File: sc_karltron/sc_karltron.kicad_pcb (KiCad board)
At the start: 2 copper layers, 88.6 x 50.6 mm, 6 parts, among them J1 Conn_01x02, J2 Conn_01x02

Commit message: basic components
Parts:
- added C1: C, Capacitor_THT:C_Disc_D5.0mm_W2.5mm_P5.00mm, F.Cu at (171.6, 25.9)
- added C2: C, Capacitor_THT:C_Disc_D5.0mm_W2.5mm_P5.00mm, F.Cu at (178.0, 10.4)
- added C3: C, Capacitor_THT:C_Disc_D5.0mm_W2.5mm_P5.00mm, F.Cu at (176.8, 18.6)
- added C4: C, Capacitor_THT:C_Disc_D5.0mm_W2.5mm_P5.00mm, F.Cu at (162.8, 29.9)
- added C5: C, Capacitor_THT:C_Disc_D5.0mm_W2.5mm_P5.00mm, F.Cu at (163.4, 25.9)
- added C6: C_Polarized, Capacitor_THT:CP_Radial_D5.0mm_P2.50mm, F.Cu at (152.5, 39.3)
- added R1: 100K, Resistor_THT:R_Axial_DIN0207_L6.3mm_D2.5mm_P10.16mm_Horizontal, F.Cu at (138.7, 49.5)
- added R10: 100K, Resistor_THT:R_Axial_DIN0207_L6.3mm_D2.5mm_P10.16mm_Horizontal, F.Cu at (164.7, 14.5)
- added R11: LDR, Resistor_THT:R_Axial_DIN0207_L6.3mm_D2.5mm_P10.16mm_Horizontal, F.Cu at (122.9, 33.2)
- added R12: 10K, Resistor_THT:R_Axial_DIN0207_L6.3mm_D2.5mm_P10.16mm_Horizontal, F.Cu at (136.8, 21.9)
- added R13: 100K, Resistor_THT:R_Axial_DIN0207_L6.3mm_D2.5mm_P10.16mm_Horizontal, F.Cu at (150.1, 21.9)
- added R14: 10K, Resistor_THT:R_Axial_DIN0207_L6.3mm_D2.5mm_P10.16mm_Horizontal, F.Cu at (125.3, 45.4)
- added R15: 100K, Resistor_THT:R_Axial_DIN0207_L6.3mm_D2.5mm_P10.16mm_Horizontal, F.Cu at (136.2, 37.3)
- added R16: 1M, Resistor_THT:R_Axial_DIN0207_L6.3mm_D2.5mm_P10.16mm_Horizontal, F.Cu at (149.5, 29.9)
- added R17: 100K, Resistor_THT:R_Axial_DIN0207_L6.3mm_D2.5mm_P10.16mm_Horizontal, F.Cu at (122.9, 41.4)
- added R18: 1M, Resistor_THT:R_Axial_DIN0207_L6.3mm_D2.5mm_P10.16mm_Horizontal, F.Cu at (112.0, 49.2)
- added R19: 100K, Resistor_THT:R_Axial_DIN0207_L6.3mm_D2.5mm_P10.16mm_Horizontal, F.Cu at (150.1, 25.9)
- added R2: 100K, Resistor_THT:R_Axial_DIN0207_L6.3mm_D2.5mm_P10.16mm_Horizontal, F.Cu at (138.7, 41.4)
- added R20: 1M, Resistor_THT:R_Axial_DIN0207_L6.3mm_D2.5mm_P10.16mm_Horizontal, F.Cu at (125.3, 49.5)
- added R3: 100K, Resistor_THT:R_Axial_DIN0207_L6.3mm_D2.5mm_P10.16mm_Horizontal, F.Cu at (122.9, 37.3)
- added R4: LDR, Resistor_THT:R_Axial_DIN0207_L6.3mm_D2.5mm_P10.16mm_Horizontal, F.Cu at (163.4, 21.9)
- added R5: 10K, Resistor_THT:R_Axial_DIN0207_L6.3mm_D2.5mm_P10.16mm_Horizontal, F.Cu at (136.2, 33.2)
- added R6: 100K, Resistor_THT:R_Axial_DIN0207_L6.3mm_D2.5mm_P10.16mm_Horizontal, F.Cu at (138.7, 45.4)
- added R7: 10K, Resistor_THT:R_Axial_DIN0207_L6.3mm_D2.5mm_P10.16mm_Horizontal, F.Cu at (136.8, 25.9)
- added R8: LDR, Resistor_THT:R_Axial_DIN0207_L6.3mm_D2.5mm_P10.16mm_Horizontal, F.Cu at (164.7, 10.4)
- added R9: 10K, Resistor_THT:R_Axial_DIN0207_L6.3mm_D2.5mm_P10.16mm_Horizontal, F.Cu at (149.5, 34.0)
- added RV1: B100K, Potentiometer_THT:Potentiometer_ACP_CA9-V10_Vertical, F.Cu at (151.2, 16.6)
- added RV2: B100K, Potentiometer_THT:Potentiometer_ACP_CA9-V10_Vertical, F.Cu at (123.3, 16.6)
- added RV3: B100K, Potentiometer_THT:Potentiometer_ACP_CA9-V10_Vertical, F.Cu at (137.2, 16.6)
- added RV4: B100K, Potentiometer_THT:Potentiometer_ACP_CA9-V10_Vertical, F.Cu at (123.3, 28.0)
- added U1: TL074, Package_DIP:DIP-14_W7.62mm, F.Cu at (112.1, 29.9)
- added U2: TL074, Package_DIP:DIP-14_W7.62mm, F.Cu at (112.1, 10.5)

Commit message: working too
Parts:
- added D1: LED, LED_THT:LED_D5.0mm_Horizontal_O3.81mm_Z3.0mm, F.Cu at (107.6, 73.2)
- added D2: LED, LED_THT:LED_D5.0mm_Horizontal_O3.81mm_Z3.0mm, F.Cu at (116.0, 73.2)
- added D3: LED, LED_THT:LED_D5.0mm_Horizontal_O3.81mm_Z3.0mm, F.Cu at (126.5, 73.7)
- added J3: In1, Connector_PinHeader_2.54mm:PinHeader_1x02_P2.54mm_Vertical, F.Cu at (216.6, 16.5)
- added J4: Out1, Connector_PinHeader_2.54mm:PinHeader_1x02_P2.54mm_Vertical, F.Cu at (227.7, 16.5)
- added J5: Out2, Connector_PinHeader_2.54mm:PinHeader_1x02_P2.54mm_Vertical, F.Cu at (190.3, 48.1)
- added J6: In2, Connector_PinHeader_2.54mm:PinHeader_1x02_P2.54mm_Vertical, F.Cu at (205.4, 16.5)
- added J7: Out3, Connector_PinHeader_2.54mm:PinHeader_1x02_P2.54mm_Vertical, F.Cu at (227.7, 31.7)
- added J8: Out4, Connector_PinHeader_2.54mm:PinHeader_1x02_P2.54mm_Vertical, F.Cu at (238.8, 16.5)
- added J9: In3, Connector_PinHeader_2.54mm:PinHeader_1x02_P2.54mm_Vertical, F.Cu at (181.5, 45.4)
- added R21: RLED, Resistor_THT:R_Axial_DIN0207_L6.3mm_D2.5mm_P10.16mm_Horizontal, F.Cu at (104.2, 84.4)
- added R22: RLED, Resistor_THT:R_Axial_DIN0207_L6.3mm_D2.5mm_P10.16mm_Horizontal, F.Cu at (113.0, 84.1)
- added R23: RLED, Resistor_THT:R_Axial_DIN0207_L6.3mm_D2.5mm_P10.16mm_Horizontal, F.Cu at (123.2, 84.2)
- added RV5: B100K, Potentiometer_THT:Potentiometer_Alpha_RD901F-40-00D_Single_Vertical, F.Cu at (147.4, 70.0)
- added RV6: B100K, Potentiometer_THT:Potentiometer_Alpha_RD901F-40-00D_Single_Vertical, F.Cu at (177.9, 98.2)
- added RV7: B100K, Potentiometer_THT:Potentiometer_Alpha_RD901F-40-00D_Single_Vertical, F.Cu at (163.5, 70.4)
- added RV8: B100K, Potentiometer_THT:Potentiometer_Alpha_RD901F-40-00D_Single_Vertical, F.Cu at (178.6, 70.7)
- C4, C5: value C -> 100nF
- C6: value C_Polarized -> 10uF
- J1, J2: footprint Connector_PinHeader_2.54mm:PinHeader_1x02_P2.54mm_Vertical -> Connector_PinHeader_2.54mm:PinHeader_1x02_P2.54mm_Horizontal
- R11, R4, R8: footprint Resistor_THT:R_Axial_DIN0207_L6.3mm_D2.5mm_P10.16mm_Horizontal -> Resistor_THT:R_Axial_DIN0204_L3.6mm_D1.6mm_P5.08mm_Horizontal
- RV1, RV2, RV3, RV4: footprint Potentiometer_THT:Potentiometer_ACP_CA9-V10_Vertical -> Potentiometer_THT:Potentiometer_ACP_CA9-H5_Horizontal
- moved R8 88.7 mm to (125.4, 90.0)
- moved U2 85.5 mm to (120.7, 95.6)
- moved R4 82.9 mm to (115.8, 89.8)
- moved U1 79.5 mm to (158.1, 94.8)
- moved C6 75.3 mm to (144.4, 114.2), turned to 90 degrees
- moved R3 69.8 mm to (88.5, 98.0)
- moved R11 58.6 mm to (106.1, 89.4)
- moved RV1 57.4 mm to (201.5, 44.2)
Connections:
- C4 pad 1: unconnected-(C4-Pad1) -> +9V
- C4 pad 2: unconnected-(C4-Pad2) -> GND
- C5 pad 1: unconnected-(C5-Pad1) -> +9V
- C5 pad 2: unconnected-(C5-Pad2) -> GND
- C6 pad 1: unconnected-(C6-Pad1) -> +9V
- C6 pad 2: unconnected-(C6-Pad2) -> GND
- R1 pad 1: unconnected-(R1-Pad1) -> Out1
- R1 pad 2: unconnected-(R1-Pad2) -> Net-(R3-Pad2)
- R14 pad 1: unconnected-(R14-Pad1) -> VMID
- R14 pad 2: unconnected-(R14-Pad2) -> GND
- R2 pad 1: unconnected-(R2-Pad1) -> Out2
- R2 pad 2: unconnected-(R2-Pad2) -> Net-(R3-Pad2)
- R3 pad 1: unconnected-(R3-Pad1) -> Out3
- R3 pad 2: unconnected-(R3-Pad2) -> Net-(R3-Pad2)
- R7 pad 1: unconnected-(R7-Pad1) -> +9V
- R7 pad 2: unconnected-(R7-Pad2) -> VMID
- RV4 pad 1: unconnected-(RV4-Pad1) -> Out4
- RV4 pad 2: unconnected-(RV4-Pad2) -> Net-(R3-Pad2)
- RV4 pad 3: unconnected-(RV4-Pad3) -> Net-(R3-Pad2)
- U1 pad 11: unconnected-(U1-Pad11) -> GND
- U1 pad 4: unconnected-(U1-Pad4) -> +9V
- U2 pad 11: unconnected-(U2-Pad11) -> GND
- U2 pad 12: unconnected-(U2-Pad12) -> VMID
- U2 pad 13: unconnected-(U2-Pad13) -> VREF
- U2 pad 14: unconnected-(U2-Pad14) -> VREF
- U2 pad 4: unconnected-(U2-Pad4) -> +9V
- U2 pad 5: unconnected-(U2-Pad5) -> VREF
- U2 pad 6: unconnected-(U2-Pad6) -> Net-(R3-Pad2)
- U2 pad 7: unconnected-(U2-Pad7) -> Out4

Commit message: halfway done
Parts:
- removed RV1, RV2, RV3, RV4: B100K, Potentiometer_THT:Potentiometer_ACP_CA9-H5_Horizontal
- added R24: 100K, Resistor_THT:R_Axial_DIN0207_L6.3mm_D2.5mm_P10.16mm_Horizontal, F.Cu at (166.5, 84.9)
- added R25: 1M, Resistor_THT:R_Axial_DIN0207_L6.3mm_D2.5mm_P10.16mm_Horizontal, F.Cu at (138.6, 97.9)
- added R26: 1M, Resistor_THT:R_Axial_DIN0207_L6.3mm_D2.5mm_P10.16mm_Horizontal, F.Cu at (167.9, 112.3)
- J1, J2: footprint Connector_PinHeader_2.54mm:PinHeader_1x02_P2.54mm_Horizontal -> Connector_PinHeader_2.54mm:PinHeader_1x02_P2.54mm_Vertical
- R16: value 1M -> 10K
- R17: value 100K -> 10K
- R18: value 1M -> 100K
- R4, R8: value LDR -> 1K; footprint Resistor_THT:R_Axial_DIN0204_L3.6mm_D1.6mm_P5.08mm_Horizontal -> Resistor_THT:R_Axial_DIN0207_L6.3mm_D2.5mm_P10.16mm_Horizontal
- R5: value 10K -> 1K
- R6: value 100K -> LDR; footprint Resistor_THT:R_Axial_DIN0207_L6.3mm_D2.5mm_P10.16mm_Horizontal -> Resistor_THT:R_Axial_DIN0204_L3.6mm_D1.6mm_P5.08mm_Horizontal
- R9: value 10K -> LDR; footprint Resistor_THT:R_Axial_DIN0207_L6.3mm_D2.5mm_P10.16mm_Horizontal -> Resistor_THT:R_Axial_DIN0204_L3.6mm_D1.6mm_P5.08mm_Horizontal
- moved J3 118.7 mm to (110.2, 69.2), turned to -90 degrees
- moved R10 102.2 mm to (117.8, 105.3), turned to 90 degrees
- moved J6 100.1 mm to (120.4, 69.3), turned to -90 degrees
- moved J8 98.6 mm to (185.6, 99.5)
- moved C1 98.3 mm to (117.3, 107.8), turned to 180 degrees
- moved C5 96.9 mm to (117.4, 111.2), turned to 180 degrees
- moved R3 93.0 mm to (181.4, 93.8), turned to 180 degrees
- moved C2 91.8 mm to (139.6, 93.8), turned to 180 degrees
- moved R13 87.7 mm to (134.0, 108.1), turned to 90 degrees
- moved R12 86.6 mm to (113.6, 105.3), turned to 90 degrees
- moved R16 85.2 mm to (109.7, 105.3), turned to 90 degrees
- moved R19 82.2 mm to (148.0, 108.1), turned to 90 degrees
- moved C4 81.8 mm to (154.5, 111.3), turned to 180 degrees
- moved C3 80.8 mm to (147.2, 93.7)
- moved J4 79.7 mm to (185.6, 84.2)
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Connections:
- C1 pad 1: unconnected-(C1-Pad1) -> Tri1
- C1 pad 2: unconnected-(C1-Pad2) -> VREF
- C2 pad 1: unconnected-(C2-Pad1) -> Tri2
- C2 pad 2: unconnected-(C2-Pad2) -> VREF
- C3 pad 1: unconnected-(C3-Pad1) -> Tri3
- C3 pad 2: unconnected-(C3-Pad2) -> VREF
- J3 pad 1: (no net) -> Net-(D1-Pad2)
- J3 pad 2: (no net) -> GND
- J4 pad 1: (no net) -> Out1
- J4 pad 2: (no net) -> GND
- J5 pad 1: (no net) -> Out2
- J5 pad 2: (no net) -> GND
- J6 pad 1: (no net) -> Net-(D2-Pad2)
- J6 pad 2: (no net) -> GND
- J7 pad 1: (no net) -> Out3
- J7 pad 2: (no net) -> GND
- J8 pad 1: (no net) -> Out4
- J8 pad 2: (no net) -> GND
- J9 pad 1: (no net) -> Net-(D3-Pad2)
- J9 pad 2: (no net) -> GND
- R10 pad 1: unconnected-(R10-Pad1) -> Net-(U1-Pad5)
- R10 pad 2: unconnected-(R10-Pad2) -> Net-(U1-Pad7)
- R11 pad 1: unconnected-(R11-Pad1) -> Net-(RV1-Pad1)
- R11 pad 2: unconnected-(R11-Pad2) -> Net-(RV1-Pad3)
- R12 pad 1: unconnected-(R12-Pad1) -> VREF
- R12 pad 2: unconnected-(R12-Pad2) -> Net-(R19-Pad1)
- R13 pad 1: unconnected-(R13-Pad1) -> Net-(R20-Pad2)
- R13 pad 2: unconnected-(R13-Pad2) -> Tri1
- R15 pad 1: unconnected-(R15-Pad1) -> Net-(U2-Pad3)
- R15 pad 2: unconnected-(R15-Pad2) -> Net-(U2-Pad1)
- R16 pad 1: unconnected-(R16-Pad1) -> VREF
- R16 pad 2: unconnected-(R16-Pad2) -> Net-(U1-Pad5)
- R17 pad 1: unconnected-(R17-Pad1) -> VREF
- R17 pad 2: unconnected-(R17-Pad2) -> Net-(U2-Pad3)
- R18 pad 1: unconnected-(R18-Pad1) -> Net-(U1-Pad13)
- R18 pad 2: unconnected-(R18-Pad2) -> Tri2
- R19 pad 1: unconnected-(R19-Pad1) -> Net-(R19-Pad1)
- R19 pad 2: unconnected-(R19-Pad2) -> Net-(RV1-Pad3)
- R20 pad 1: unconnected-(R20-Pad1) -> Out1
- R20 pad 2: unconnected-(R20-Pad2) -> Net-(R20-Pad2)
- R4 pad 1: unconnected-(R4-Pad1) -> Tri1
- R4 pad 2: unconnected-(R4-Pad2) -> Net-(RV1-Pad1)
- R5 pad 1: unconnected-(R5-Pad1) -> Tri2
- R5 pad 2: unconnected-(R5-Pad2) -> Net-(R5-Pad2)
- R6 pad 1: unconnected-(R6-Pad1) -> Net-(R5-Pad2)
- R6 pad 2: unconnected-(R6-Pad2) -> Net-(U1-Pad7)
- R8 pad 1: unconnected-(R8-Pad1) -> Tri3
- R8 pad 2: unconnected-(R8-Pad2) -> Net-(R8-Pad2)
- R9 pad 1: unconnected-(R9-Pad1) -> Net-(R8-Pad2)
- R9 pad 2: unconnected-(R9-Pad2) -> Net-(U2-Pad1)
- RV5 pad 1: unconnected-(RV5-Pad1) -> Net-(RV1-Pad1)
- RV5 pad 2: unconnected-(RV5-Pad2) -> Net-(RV1-Pad1)
- RV5 pad 3: unconnected-(RV5-Pad3) -> Net-(RV1-Pad3)
- RV6 pad 1: unconnected-(RV6-Pad1) -> Net-(R5-Pad2)
- RV6 pad 2: unconnected-(RV6-Pad2) -> Net-(R5-Pad2)
- RV6 pad 3: unconnected-(RV6-Pad3) -> Net-(U1-Pad7)
- RV7 pad 1: unconnected-(RV7-Pad1) -> Net-(R8-Pad2)
- RV7 pad 2: unconnected-(RV7-Pad2) -> Net-(R8-Pad2)
- RV7 pad 3: unconnected-(RV7-Pad3) -> Net-(U2-Pad1)
- U1 pad 1: unconnected-(U1-Pad1) -> Net-(RV1-Pad3)
- U1 pad 10: unconnected-(U1-Pad10) -> VREF
- U1 pad 12: unconnected-(U1-Pad12) -> VREF
- U1 pad 13: unconnected-(U1-Pad13) -> Net-(U1-Pad13)
- U1 pad 14: unconnected-(U1-Pad14) -> Out2
- U1 pad 2: unconnected-(U1-Pad2) -> Tri1
- U1 pad 3: unconnected-(U1-Pad3) -> Net-(R19-Pad1)
- U1 pad 5: unconnected-(U1-Pad5) -> Net-(U1-Pad5)
- U1 pad 6: unconnected-(U1-Pad6) -> Tri2
- U1 pad 7: unconnected-(U1-Pad7) -> Net-(U1-Pad7)
- U1 pad 8: unconnected-(U1-Pad8) -> Out1
- U1 pad 9: unconnected-(U1-Pad9) -> Net-(R20-Pad2)
- U2 pad 1: unconnected-(U2-Pad1) -> Net-(U2-Pad1)
- U2 pad 10: unconnected-(U2-Pad10) -> VREF
- U2 pad 2: unconnected-(U2-Pad2) -> Tri3
- U2 pad 3: unconnected-(U2-Pad3) -> Net-(U2-Pad3)
- U2 pad 8: unconnected-(U2-Pad8) -> Out3
- U2 pad 9: unconnected-(U2-Pad9) -> Net-(U2-Pad9)
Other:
- board text added: "1"
- board text added: "2"
- board text added: "3"
- board text added: "B100K"

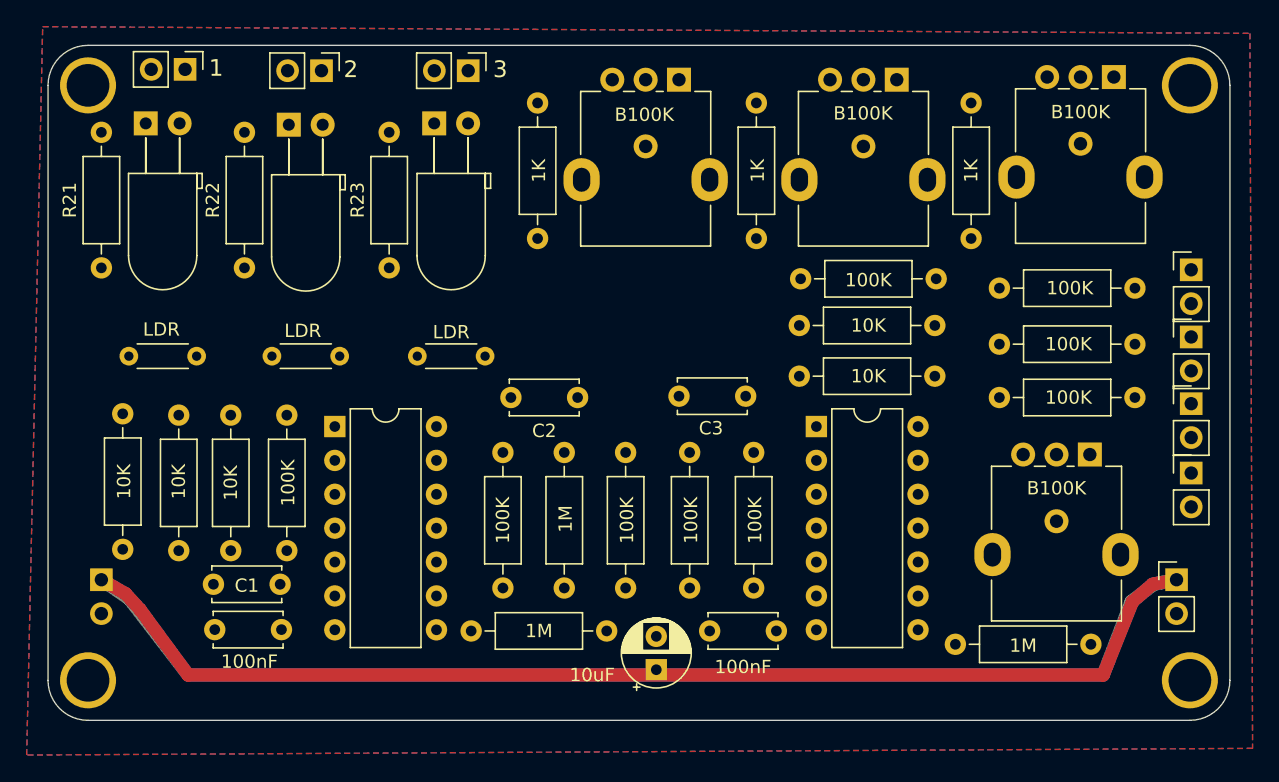
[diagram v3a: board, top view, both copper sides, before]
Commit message: completing
v1.0 looks good to order. still untested
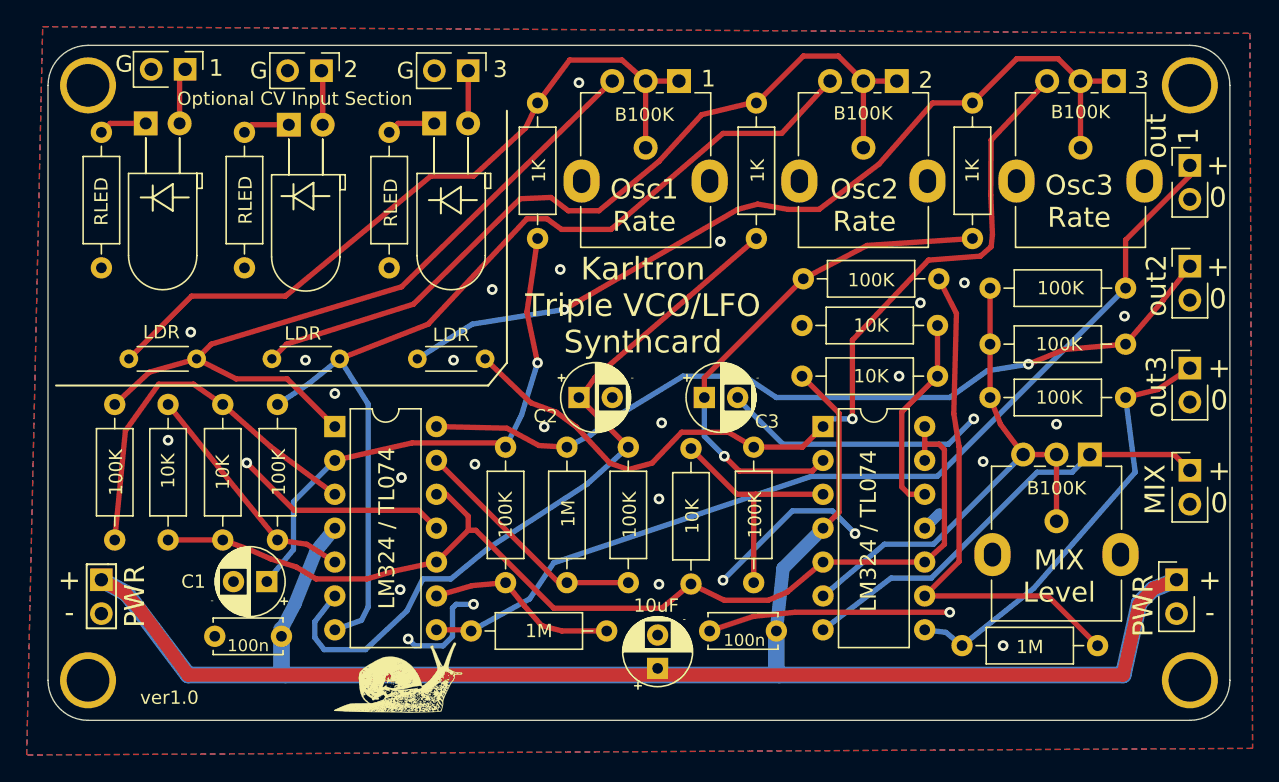
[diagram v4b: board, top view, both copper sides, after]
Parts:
- added G***: LOGO, sna:snail4.sm, F.Cu at (126.4, 114.6)
- added G***: LOGO, sna:sine, B.Cu at (125.2, 106.9)
- added G***: LOGO, sna:snail4, B.Cu at (169.4, 112.0)
- added G***: LOGO, sna:sine, B.Cu at (175.4, 92.1)
- added G***: LOGO, sna:sine, B.Cu at (125.2, 99.9)
- C1, C2, C3: footprint Capacitor_THT:C_Disc_D5.0mm_W2.5mm_P5.00mm -> Capacitor_THT:CP_Radial_D5.0mm_P2.50mm
- C4, C5: value 100nF -> 100n
- moved R19 43.3 mm to (104.9, 104.5)
- moved R17 42.7 mm to (148.1, 107.8)
- moved J4 7.83 mm to (185.5, 76.4)
- moved J5 5.30 mm to (185.5, 84.0)
- moved J7 2.66 mm to (185.5, 91.6)
- moved C3 1.90 mm to (149.1, 93.8)
- moved R16 1.13 mm to (108.9, 104.5)
- moved R10 1.06 mm to (117.1, 104.5)
- moved C1 1.01 mm to (116.3, 107.6)
- moved R12 1.00 mm to (113.0, 104.5)
- moved R1 0.70 mm to (180.7, 85.6)
- moved R2 0.70 mm to (180.7, 89.8)
- moved R3 0.70 mm to (180.7, 93.8)
- moved R26 0.51 mm to (168.4, 112.4)
- moved C5 0.50 mm to (117.4, 111.7)
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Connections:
- C1 pad 2: VREF -> GND
- C2 pad 2: VREF -> GND
- C3 pad 2: VREF -> GND
- RV5 pad : (no net) -> GND
- RV6 pad : (no net) -> GND
- RV7 pad : (no net) -> GND
- RV8 pad : (no net) -> GND
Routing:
- net VREF: track 0.00 -> 80.2 mm
- net GND: track 0.00 -> 76.3 mm, vias 0 -> 30
- net Net-(U1-Pad7): track 0.00 -> 73.6 mm
- net Out1: track 0.00 -> 71.9 mm
- net Net-(U2-Pad1): track 0.00 -> 66.1 mm, vias 0 -> 1
- net Net-(R8-Pad2): track 0.00 -> 65.4 mm, vias 0 -> 1
- net Out2: track 0.00 -> 62.5 mm, vias 0 -> 1
- net Net-(R5-Pad2): track 0.00 -> 61.5 mm
- net Net-(RV1-Pad3): track 0.00 -> 58.0 mm
- net Tri2: track 0.00 -> 56.6 mm
- net Net-(RV1-Pad1): track 0.00 -> 56.2 mm
- net Tri1: track 0.00 -> 40.4 mm, vias 0 -> 1
- net Net-(R3-Pad2): track 0.00 -> 39.9 mm
- net Net-(U2-Pad9): track 0.00 -> 39.7 mm
- net Tri3: track 0.00 -> 38.5 mm, vias 0 -> 1
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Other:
- board text added: "+ -"
- board text added: "+ 0"
- board text added: "-"
- board text added: "Don't be scared to try it!"
- board text added: "Eurorack made in Wisconsin DIY-friendly synth system"
- board text added: "G"
- board text added: "JLCJLCJLCJLC"
- board text added: "Karltron Synthesizers"
- board text added: "Karltron Triple VCO/LFO Synthcard"
- board text added: "LM324 / TL074"
- board text added: "MIX"
- board text added: "MIX Level"
- board text added: "Optional CV Input Section"
- board text added: "Osc1 Rate"
- board text added: "Osc2 Rate"
- board text added: "Osc3 Rate"
- board text added: "PWR"
- board text added: "email info@karltron.com"
- board text added: "github.com/SynthCard"
- board text added: "github.com/kstammits"
- board text added: "instagram.com/karltronsynth"
- board text added: "join the SynthCard project at synthcard.com"
- board text added: "karltron.com/synthcard"
- board text added: "listen at"
- board text added: "out 1"
- board text added: "out2"
- board text added: "out3"
- board text added: "this card becomes a real VCO/LFO"
- board text added: "ver1.0"

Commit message: adding notes
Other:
- board text added: "file not tested physically i still need to order one and build it before i can guarantee this board is good"
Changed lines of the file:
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@@
     (effects (font (size 1.5 1.5) (thickness 0.2)))
+  )
+  (gr_text "file not tested physically\ni still need to order one and build it \n  before i can guarantee this board is good" (at 144.1 49.7) (layer "Cmts.User")
+    (effects (font (size 2 2) (thickness 0.2)))
   )
   (dimension (type aligned) (layer "Dwgs.User")
